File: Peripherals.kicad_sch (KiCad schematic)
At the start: 0 parts

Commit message: [#81970] Finalize connecting SFP+ to SOM
[#82054] Update SoM pins definitions

[#82054] Continue work on I2C

[#82330] Clean up

[#81970] Add SFP sheet and power section

[#82330] Annotation and clean up
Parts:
- added C130, C44, C48: C_100n_0402, antmicro-footprints:C_0402_1005Metric, symbol antmicroCapacitors0402:C_100n_0402
- added D26, D27, D54: LED_G_0603_LTST-C190GKT, antmicro-footprints:LED_0603_1608Metric_G, symbol antmicroLEDIndicationDiscrete:LED_G_0603_LTST-C190GKT
- added D56, D57, D58, D59: TPD1E0B04_XDFN-2, antmicro-footprints:XDFN-2_1x0.60mm, symbol antmicroTVSDiodes:TPD1E0B04_XDFN-2
- added D63: RB521S30T1G, antmicro-footprints:SOD-523, symbol antmicroDiodesRectifiersSingle:RB521S30T1G
- added J10: Molex_PicoBlade_1x4_0533980471, antmicro-footprints:Conn_Molex_PicoBlade_1x4_0533980471, symbol antmicroWire2BoardConnectors:Molex_PicoBlade_1x4_0533980471
- added J14: JST_SH_1x4_SM04B-SRSS-TB-LF-SN, antmicro-footprints:Conn_JST_SH_1x4_SM04B-SRSS-TB-LF-SN, symbol antmicroWire2BoardConnectors:JST_SH_1x4_SM04B-SRSS-TB-LF-SN
- added J9: Tag-Connect_TC2050-IDC-NL_2x5_P1.27mm, antmicro-footprints:Tag-Connect_TC2050-IDC-NL_2x5_P1.27mm, symbol antmicroTestPoints:Tag-Connect_TC2050-IDC-NL_2x5_P1.27mm
- added Q10, Q9: PJE138K, antmicro-footprints:SOT-523, symbol antmicroTransistorsFETsMOSFETsSingle:PJE138K
- added R112: R_4x100R_0201_array, antmicro-footprints:R_Array_4x0201_Panasonic_EXB18V, symbol antmicroResistorNetworksArrays:R_4x100R_0201_array
- added R189, R232, R242: R_10k_0402, antmicro-footprints:R_0402_1005Metric, symbol antmicroResistors0402:R_10k_0402
- added R190: R_15k_0402, antmicro-footprints:R_0402_1005Metric, symbol antmicroResistors0402:R_15k_0402
- added R191, R223, R231: R_200R_0402, antmicro-footprints:R_0402_1005Metric, symbol antmicroResistors0402:R_200R_0402
- added R192, R222, R230: R_100k_0402, antmicro-footprints:R_0402_1005Metric, symbol antmicroResistors0402:R_100k_0402
- added R204: R_4x0R_0201_array, antmicro-footprints:R_Array_4x0201_Panasonic_EXB18V, symbol antmicroResistorNetworksArrays:R_4x0R_0201_array
- added S2, S3: SW_KMR211NGLFS_SMD, antmicro-footprints:SW_KMR211NGLFS_SMD, symbol antmicroPushbuttonSwitches:SW_KMR211NGLFS_SMD
- added U33: NTS0102_XSON, antmicro-footprints:XSON-8_1x1.95mm_P0.5mm, symbol antmicroLogicTranslatorsLevelShifters:NTS0102_XSON
- added U35: AP22653_DFN, antmicro-footprints:DFN-6-1EP_2x2mm_P0.65mm_EP1x1.6mm, symbol antmicroPMICPowerDistributionSwitchesLoadDrivers:AP22653_DFN
- added U49: SLB9673AU20FW2610XTMA1, antmicro-footprints:QFN-32-1EP_5x5mm, symbol antmicroInterfaceControllers:SLB9673AU20FW2610XTMA1
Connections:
- new net: D63.2 (A), R112.1 (R1.1)
- new net: D26.1 (C), Q9.3 (D)
- new net: D26.2 (A), R223.1
- new net: D54.2 (A), R191.1
- new net: D27.1 (C), Q10.3 (D)
- new net: D27.2 (A), R231.1
- new net: R190.2, U35.2 (ISET)
- new net: U49.1 (VDD), U49.14 (VDD), U49.22 (VDD)
- new net: U49.2 (GND), U49.23 (GND), U49.32 (GND), U49.9 (GND)
- new net +1V8: C44.2, R232.2, R242.2, U33.3 (VCC_{A}), U33.6 (OE)
- new net +3V3: C130.1, R189.2, R223.2, R231.2, U35.6 (IN)
- new net +5V: C48.2, J10.2, U33.7 (VCC_{B})
- new net EEPROM_PWR: J9.1
- new net FAN_PWM: U33.5 (A_{1})
- new net FAN_PWM_5V: J10.4, U33.8 (B_{1})
- new net FAN_TACH: U33.4 (A_{2})
- new net FAN_TACH_5V: J10.3, U33.1 (B_{2})
- new net GND: C130.2, C44.1, C48.1, D54.1 (C), D56.1 (C), D57.1 (C), D58.1 (C), D59.1 (C), J10.1, J14.1, J14.MP, J9.3, J9.5, J9.9, Q10.2 (S), Q9.2 (S), R190.1, R192.1, R222.1, R230.1, S2.3, S2.4, S3.3, S3.4, U33.2 (GND), U35.5 (GND), U35.7 (EP)
- new net I2C1_SCL: D56.2 (A), J14.4
- new net I2C1_SDA: D57.2 (A), J14.3
- new net I2C_CONN_3V3: J14.2, R191.2, U35.1 (OUT)
- new net I2C_CONN_PEN: R189.1, R192.2, U35.4 (EN)
- new net MISO: J9.6, R112.2 (R2.1), R204.4 (R4.1)
- new net MOSI: J9.8, R112.3 (R3.1), R204.2 (R2.1)
- new net PDC_MISO: R204.5 (R4.2)
- new net PDC_MOSI: R204.7 (R2.2)
- new net PDC_SCLK: R204.6 (R3.2)
- new net SCK: D63.1 (C), J9.4, R204.3 (R3.1)
- new net SYS_SCL: R112.8 (R1.2)
- new net SYS_SDA: R112.6 (R3.2), R112.7 (R2.2)
- new net USER_BTN0: D58.2 (A), R232.1, S2.1, S2.2
- new net USER_BTN1: D59.2 (A), R242.1, S3.1, S3.2
- new net USER_LED0: Q9.1 (G), R222.2
- new net USER_LED1: Q10.1 (G), R230.2
- new net ~{CS}: J9.2, R204.1 (R1.1)
- new net ~{PDC_CS}: R204.8 (R1.2)
- no-connect marks 0 -> 7
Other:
- note added: "Buttons"
- note added: "Debug connector"
- note added: "Fan connector"
- note added: "I2C connector"
- note added: "LED indicators"
- note added: "pinout compatible with www.github.com/antmicro/ftdi-toolkit"

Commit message: [#82330] Add TPM
[#82330] Add ID-EEPROM

[#82055] Clean up
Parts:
- removed D63: RB521S30T1G, antmicro-footprints:SOD-523, symbol antmicroDiodesRectifiersSingle:RB521S30T1G
- removed J9: Tag-Connect_TC2050-IDC-NL_2x5_P1.27mm, antmicro-footprints:Tag-Connect_TC2050-IDC-NL_2x5_P1.27mm, symbol antmicroTestPoints:Tag-Connect_TC2050-IDC-NL_2x5_P1.27mm
- removed R112: R_4x100R_0201_array, antmicro-footprints:R_Array_4x0201_Panasonic_EXB18V, symbol antmicroResistorNetworksArrays:R_4x100R_0201_array
- removed R204: R_4x0R_0201_array, antmicro-footprints:R_Array_4x0201_Panasonic_EXB18V, symbol antmicroResistorNetworksArrays:R_4x0R_0201_array
- added C58, C59, C60: C_100n_16V_X7R_0402, antmicro-footprints:C_0402_1005Metric, symbol antmicroCapacitors0402:C_100n_16V_X7R_0402
- added C61: C_1u_16V_0402, antmicro-footprints:C_0402_1005Metric, symbol antmicroCapacitors0402:C_1u_16V_0402
- added C93: C_100n_0402, antmicro-footprints:C_0402_1005Metric, symbol antmicroCapacitors0402:C_100n_0402
- added R109, R110, R112, R114: R_0R_0402, antmicro-footprints:R_0402_1005Metric, symbol antmicroResistors0402:R_0R_0402
- added R59, R60, R61, R62: R_10k_0402, antmicro-footprints:R_0402_1005Metric, symbol antmicroResistors0402:R_10k_0402
- added U21: M24C64-F_DFN8, antmicro-footprints:DFN-8-1EP_3x2mm_P0.5mm_EP1.36x1.46mm, symbol antmicroMemory:M24C64-F_DFN8
- renumbered C44 to C56, C48 to C57, C130 to C62, D54 to D10, D27 to D11, D58 to D12, D59 to D13, D26 to D7, D56 to D8, D57 to D9, J10 to J5, J14 to J6, Q9 to Q3, Q10 to Q4, R222 to R65, R223 to R66, R189 to R67, R192 to R68, R190 to R69, R230 to R70, R191 to R71, R231 to R72, R232 to R73, R242 to R74, S2 to S1, S3 to S2, U33 to U16, U49 to U17, U35 to U18
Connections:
- net +3V3: now also U17.1 (VDD), U17.14 (VDD), U17.20 (TEST#), U17.22 (VDD), U17.8 (NCI/VDD), C58.2, C59.2, C60.2, C61.2, R59.2, R60.2, R61.2, R62.2
- net GND: now also U17.16 (NCI/GND), U17.2 (GND), U17.23 (GND), U17.32 (GND), U17.33 (EP), U17.9 (GND), C58.1, C59.1, C60.1, C61.1, C93.1, R114.1, U21.4 (VSS), U21.9 (VSS)
- net SYS_SCL: now also R109.1, U21.6 (SCL)
- net SYS_SDA: now also R110.1, U21.5 (SDA)
- net at U17.17 (RST#): now also R60.1
- net GPIO01: now reaches U17.18 (I2C_PIRQ#)
- net GPIO01: now also R59.1
- net at U17.29 (SDA): now also R61.1
- net at U17.30 (SCL): now also R62.1
- net I2C1_SCL: no longer names the net of D8.2 (A), J6.4
- net I2C1_SDA: no longer names the net of D9.2 (A), J6.3
- new net: R112.1, R114.2, U21.7 (~{WC})
- new net +3V3_AON: C93.2, R112.2, U21.1 (E0), U21.2 (E1), U21.3 (E2), U21.8 (VCC)
- new net DEBUG_SCL: R109.2
- new net DEBUG_SDA: R110.2
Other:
- note added: "ID EEPROM"
- note added: "I^{2}C"
- note added: "Status LEDs"
- note added: "TPM"
- note removed: "Debug connector"
- note removed: "I2C connector"
- note removed: "LED indicators"
- note removed: "pinout compatible with www.github.com/antmicro/ftdi-toolkit"
- moved on the sheet: C56, C57, D11, D12, D13, D7, D8, D9, J5, J6, Q3, Q4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

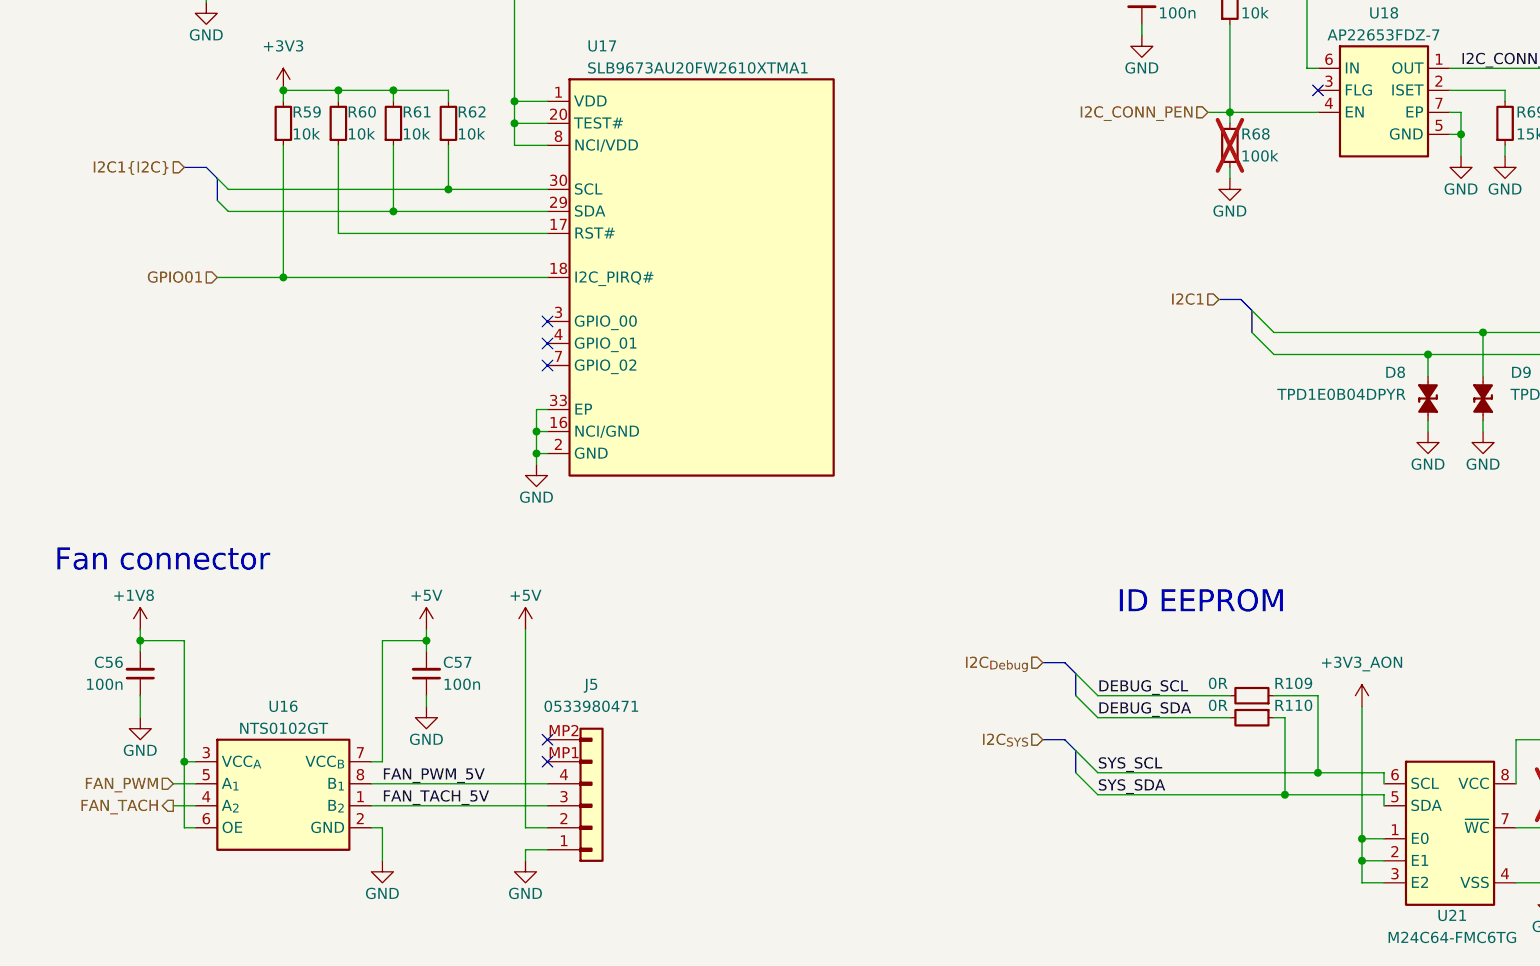
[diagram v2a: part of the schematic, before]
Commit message: [#81970] Route traces from root schematic on other schematics
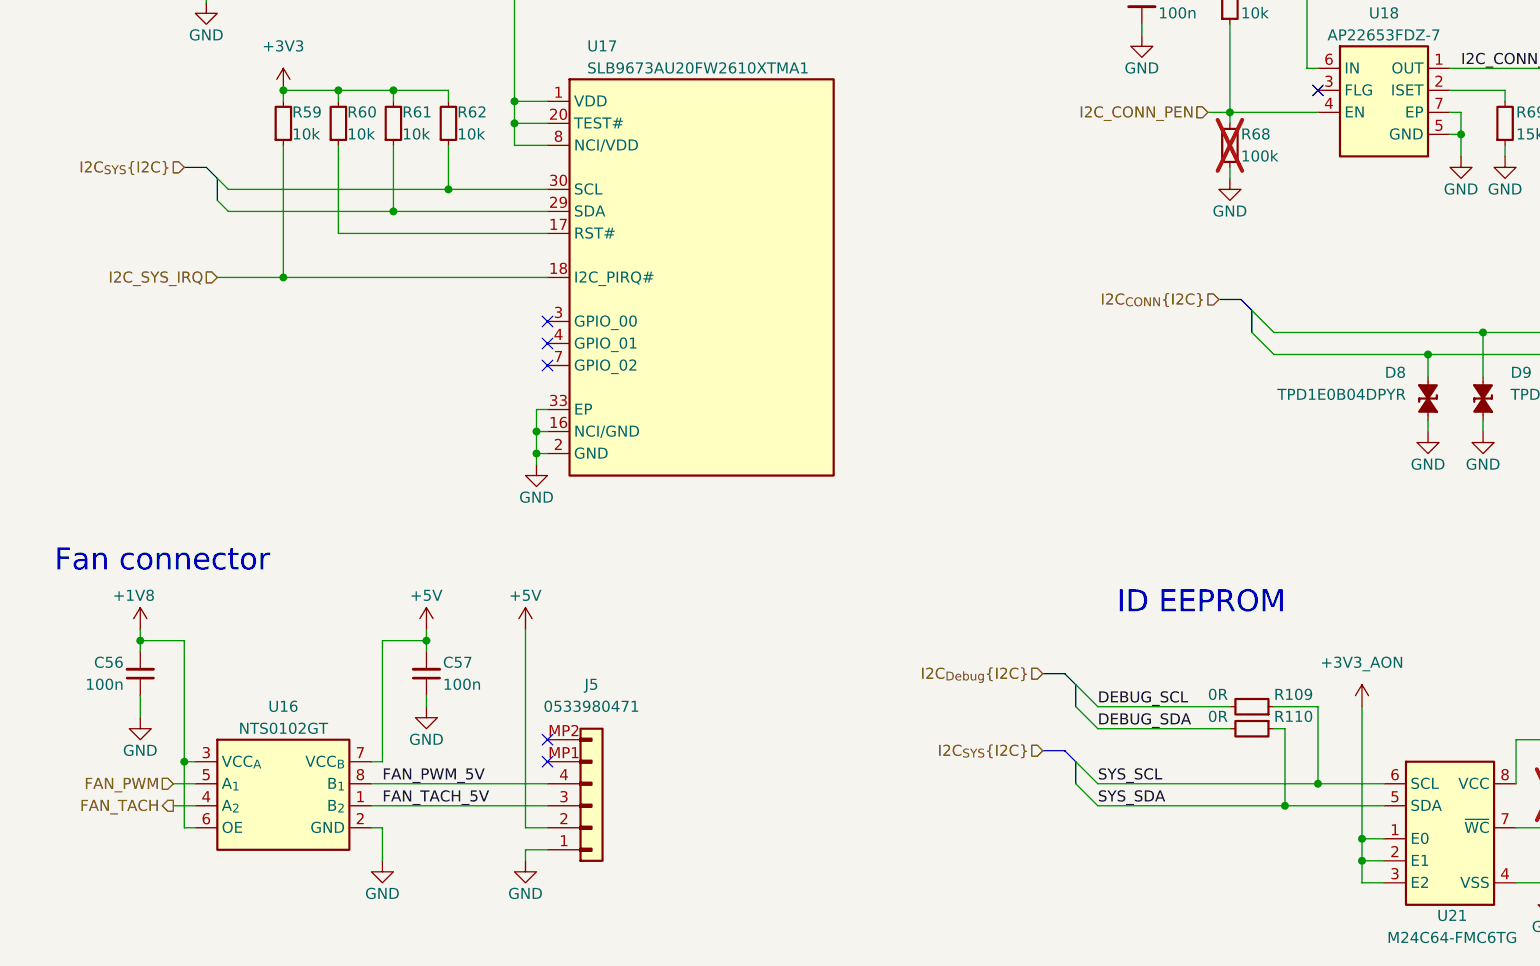
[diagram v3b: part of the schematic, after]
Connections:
- net GPIO01 renamed I2C_SYS_IRQ
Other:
- moved on the sheet: R109, R110
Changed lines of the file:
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@@
 	)
 	(junction
-		(at 172.72 130.81)
+		(at 172.72 132.08)
 		(diameter 0)
 		(color 0 0 0 0)
@@
 	)
 	(junction
-		(at 176.53 128.27)
+		(at 176.53 129.54)
 		(diameter 0)
 		(color 0 0 0 0)
@@
 	)
 	(bus_entry
-		(at 148.59 119.38)
+		(at 148.59 120.65)
 		(size 2.54 2.54)
 		(stroke
@@
 	)
 	(bus_entry
-		(at 148.59 125.73)
+		(at 148.59 127)
 		(size 2.54 2.54)
 		(stroke
@@
 	)
 	(bus_entry
-		(at 148.59 128.27)
+		(at 148.59 129.54)
 		(size 2.54 2.54)
 		(stroke
@@
 	)
 	(bus_entry
-		(at 148.59 116.84)
+		(at 148.59 118.11)
 		(size 2.54 2.54)
 		(stroke
@@
 	(wire
 		(pts
-			(xy 151.13 121.92) (xy 166.37 121.92)
+			(xy 151.13 123.19) (xy 166.37 123.19)
 		)
 		(stroke
@@
 	(wire
 		(pts
-			(xy 176.53 119.38) (xy 176.53 128.27)
+			(xy 176.53 120.65) (xy 176.53 129.54)
 		)
 		(stroke
@@
 	(wire
 		(pts
-			(xy 172.72 121.92) (xy 172.72 130.81)
+			(xy 172.72 123.19) (xy 172.72 132.08)
 		)
 		(stroke
@@
 	(bus
 		(pts
-			(xy 144.78 124.46) (xy 147.32 124.46)
+			(xy 144.78 125.73) (xy 147.32 125.73)
 		)
 		(stroke
@@
 	(bus
 		(pts
-			(xy 147.32 115.57) (xy 148.59 116.84)
+			(xy 147.32 116.84) (xy 148.59 118.11)
 		)
 		(stroke
@@
 	(wire
 		(pts
-			(xy 151.13 130.81) (xy 172.72 130.81)
+			(xy 151.13 132.08) (xy 172.72 132.08)
 		)
 		(stroke
@@
 	(wire
 		(pts
-			(xy 151.13 119.38) (xy 166.37 119.38)
+			(xy 151.13 120.65) (xy 166.37 120.65)
 		)
 		(stroke
@@
 	(bus
 		(pts
-			(xy 144.78 115.57) (xy 147.32 115.57)
+			(xy 144.78 116.84) (xy 147.32 116.84)
 		)
 		(stroke
@@
 	(bus
 		(pts
-			(xy 147.32 124.46) (xy 148.59 125.73)
+			(xy 147.32 125.73) (xy 148.59 127)
 		)
 		(stroke
@@
 	(bus
 		(pts
-			(xy 148.59 125.73) (xy 148.59 128.27)
+			(xy 148.59 127) (xy 148.59 129.54)
 		)
 		(stroke
@@
 	(wire
 		(pts
-			(xy 176.53 128.27) (xy 184.15 128.27)
+			(xy 176.53 129.54) (xy 184.15 129.54)
 		)
 		(stroke
@@
 	(bus
 		(pts
-			(xy 148.59 116.84) (xy 148.59 119.38)
+			(xy 148.59 118.11) (xy 148.59 120.65)
 		)
 		(stroke
@@
 	(wire
 		(pts
-			(xy 151.13 128.27) (xy 176.53 128.27)
+			(xy 151.13 129.54) (xy 176.53 129.54)
 		)
 		(stroke
@@
 	(wire
 		(pts
-			(xy 172.72 130.81) (xy 184.15 130.81)
+			(xy 172.72 132.08) (xy 184.15 132.08)
 		)
 		(stroke
@@
 	(wire
 		(pts
-			(xy 184.15 128.27) (xy 184.15 129.54)
-		)
-		(stroke
-			(width 0)
-			(type default)
-		)
-	)
-	(wire
-		(pts
-			(xy 171.45 119.38) (xy 176.53 119.38)
+			(xy 171.45 120.65) (xy 176.53 120.65)
 		)
 		(stroke
@@
 	(wire
 		(pts
-			(xy 184.15 130.81) (xy 184.15 132.08)
-		)
-		(stroke
-			(width 0)
-			(type default)
-		)
-	)
-	(wire
-		(pts
 			(xy 203.2 134.62) (xy 199.39 134.62)
 		)
@@
 	(wire
 		(pts
-			(xy 171.45 121.92) (xy 172.72 121.92)
+			(xy 171.45 123.19) (xy 172.72 123.19)
 		)
 		(stroke
@@
 	)
 	(label "DEBUG_SCL"
-		(at 151.13 119.38 0)
+		(at 151.13 120.65 0)
 		(effects
 			(font
@@
 	)
 	(label "DEBUG_SDA"
-		(at 151.13 121.92 0)
+		(at 151.13 123.19 0)
 		(effects
 			(font
@@
 	)
 	(label "SYS_SDA"
-		(at 151.13 130.81 0)
+		(at 151.13 132.08 0)
 		(effects
 			(font
@@
 	)
 	(label "SYS_SCL"
-		(at 151.13 128.27 0)
+		(at 151.13 129.54 0)
 		(effects
 			(font
@@
 		)
 	)
-	(hierarchical_label "I2C_{SYS}"
+	(hierarchical_label "I2C_{SYS}{I2C}"
 		(shape input)
-		(at 144.78 124.46 180)
+		(at 144.78 125.73 180)
 		(effects
 			(font
@@
 		)
 	)
-	(hierarchical_label "I2C1{I2C}"
+	(hierarchical_label "I2C_{SYS}{I2C}"
 		(shape input)
 		(at 45.72 58.42 180)
@@
 		)
 	)
-	(hierarchical_label "GPIO01"
+	(hierarchical_label "I2C_SYS_IRQ"
 		(shape input)
 		(at 49.53 71.12 180)
@@
 		)
 	)
-	(hierarchical_label "I2C_{Debug}"
+	(hierarchical_label "I2C_{Debug}{I2C}"
 		(shape input)
-		(at 144.78 115.57 180)
+		(at 144.78 116.84 180)
 		(effects
 			(font
@@
 		)
 	)
-	(hierarchical_label "I2C1"
+	(hierarchical_label "I2C_{CONN}{I2C}"
 		(shape input)
 		(at 165.1 73.66 180)
@@
 		(lib_name "R_0R_0402_5")
 		(lib_id "antmicroResistors0402:R_0R_0402")
-		(at 171.45 121.92 0)
+		(at 171.45 123.19 0)
 		(mirror y)
 		(unit 1)
@@
 		(dnp no)
 		(property "Reference" "R110"
-			(at 171.45 121.285 0)
+			(at 171.45 122.555 0)
 			(effects
 				(font
@@
 		)
 		(property "Value" "R_0R_0402"
-			(at 151.13 134.62 0)
+			(at 151.13 135.89 0)
 			(effects
 				(font
@@
 		)
 		(property "Footprint" "antmicro-footprints:R_0402_1005Metric"
-			(at 151.13 137.16 0)
+			(at 151.13 138.43 0)
 			(effects
 				(font
@@
 		)
 		(property "Datasheet" "https://industrial.panasonic.com/cdbs/www-data/pdf/RDA0000/AOA0000C301.pdf"
-			(at 151.13 139.7 0)
+			(at 151.13 140.97 0)
 			(effects
 				(font
@@
 		)
 		(property "Description" ""
-			(at 171.45 121.92 0)
+			(at 171.45 123.19 0)
 			(effects
 				(font
@@
 		)
 		(property "Manufacturer" "Panasonic"
-			(at 151.13 144.78 0)
+			(at 151.13 146.05 0)
 			(effects
 				(font
@@
 		)
 		(property "MPN" "ERJ2GE0R00X"
-			(at 151.13 142.24 0)
+			(at 151.13 143.51 0)
 			(effects
 				(font
@@
 		)
 		(property "Val" "0R"
-			(at 163.83 121.285 0)
+			(at 163.83 122.555 0)
 			(effects
 				(font
@@
 		)
 		(property "License" "Apache-2.0"
-			(at 151.13 147.32 0)
+			(at 151.13 148.59 0)
 			(effects
 				(font
@@
 		)
 		(property "Author" "Antmicro"
-			(at 151.13 149.86 0)
+			(at 151.13 151.13 0)
 			(effects
 				(font
@@
 		)
 		(property "Tolerance" "~"
-			(at 151.13 132.08 0)
+			(at 151.13 133.35 0)
 			(effects
 				(font
@@
 		)
 		(property "Current" "1A"
-			(at 151.13 152.4 0)
+			(at 151.13 153.67 0)
 			(effects
 				(font
@@
 		(lib_name "R_0R_0402_2")
 		(lib_id "antmicroResistors0402:R_0R_0402")
-		(at 171.45 119.38 180)
+		(at 171.45 120.65 180)
 		(unit 1)
 		(exclude_from_sim no)
@@
 		(dnp no)
 		(property "Reference" "R109"
-			(at 171.45 118.745 0)
+			(at 171.45 120.015 0)
 			(effects
 				(font
@@
 		)
 		(property "Value" "R_0R_0402"
-			(at 151.13 106.68 0)
+			(at 151.13 107.95 0)
 			(effects
 				(font
@@
 		)
 		(property "Footprint" "antmicro-footprints:R_0402_1005Metric"
-			(at 151.13 104.14 0)
+			(at 151.13 105.41 0)
 			(effects
 				(font
@@
 		)
 		(property "Datasheet" "https://industrial.panasonic.com/cdbs/www-data/pdf/RDA0000/AOA0000C301.pdf"
-			(at 151.13 101.6 0)
+			(at 151.13 102.87 0)
 			(effects
 				(font
@@
 		)
 		(property "Description" ""
-			(at 171.45 119.38 0)
+			(at 171.45 120.65 0)
 			(effects
 				(font
@@
 		)
 		(property "Manufacturer" "Panasonic"
-			(at 151.13 96.52 0)
+			(at 151.13 97.79 0)
 			(effects
 				(font
@@
 		)
 		(property "MPN" "ERJ2GE0R00X"
-			(at 151.13 99.06 0)
+			(at 151.13 100.33 0)
 			(effects
 				(font
@@
 		)
 		(property "Val" "0R"
-			(at 163.83 118.745 0)
+			(at 163.83 120.015 0)
 			(effects
 				(font
@@
 		)
 		(property "License" "Apache-2.0"
-			(at 151.13 93.98 0)
+			(at 151.13 95.25 0)
 			(effects
 				(font
@@
 		)
 		(property "Author" "Antmicro"
-			(at 151.13 91.44 0)
+			(at 151.13 92.71 0)
 			(effects
 				(font
@@
 		)
 		(property "Tolerance" "~"
-			(at 151.13 109.22 0)
+			(at 151.13 110.49 0)
 			(effects
 				(font
@@
 		)
 		(property "Current" "1A"
-			(at 151.13 88.9 0)
+			(at 151.13 90.17 0)
 			(effects
 				(font
